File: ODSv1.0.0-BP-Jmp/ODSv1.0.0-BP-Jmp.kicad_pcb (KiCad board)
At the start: 2 copper layers, 150 x 150 mm, 56 parts, among them J1 Conn_01x16, J10 Conn_02x10_Odd_Even, J11 Conn_02x10_Odd_Even, J12 Conn_02x10_Odd_Even, J13 Conn_02x10_Odd_Even, J14 Conn_02x10_Odd_Even, J15 Conn_02x10_Odd_Even, J16 Conn_02x10_Odd_Even, J17 Conn_02x10_Odd_Even, J2 Conn_02x60_Odd_Even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

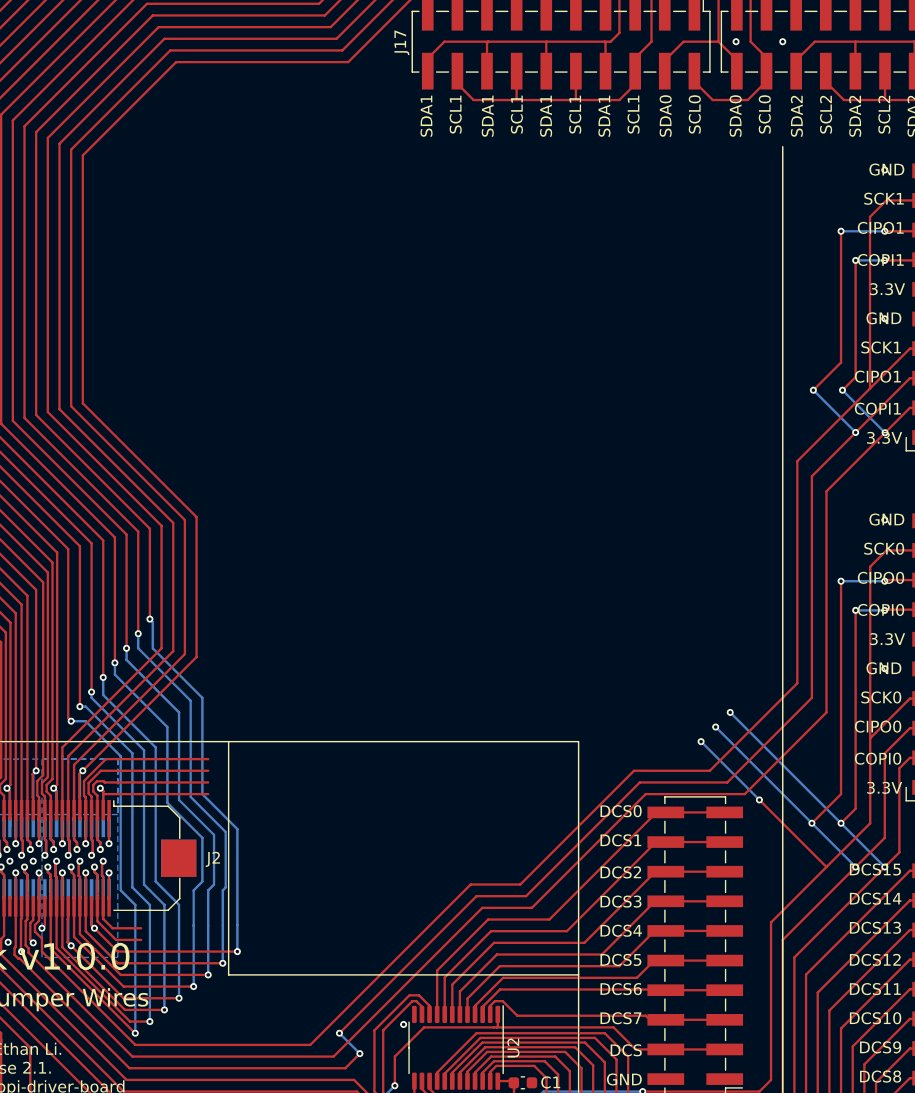
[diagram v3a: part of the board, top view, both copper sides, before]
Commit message: Finish routing I2C headers
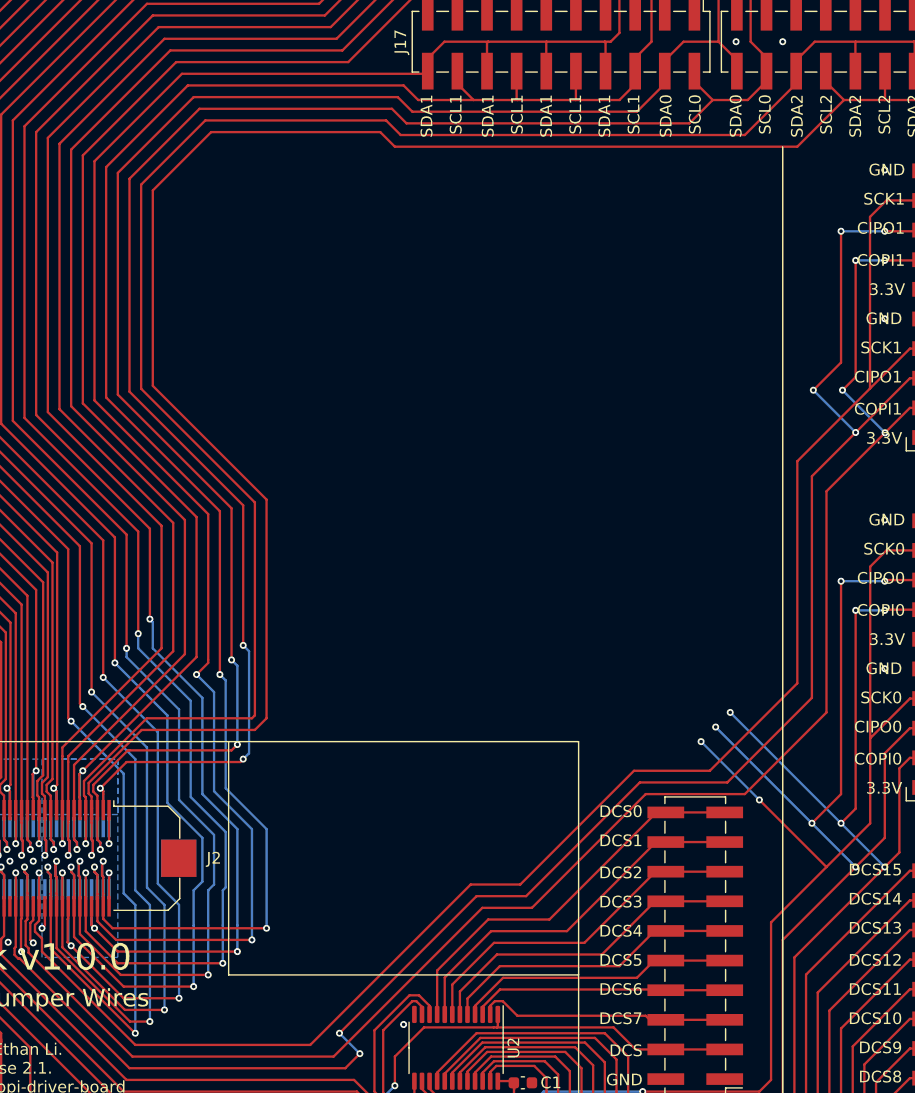
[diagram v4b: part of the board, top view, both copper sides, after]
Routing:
- net /Backbone/I2C2_SCL: track 59.5 -> 179.2 mm
- net /Backbone/I2C2_SDA: track 60.4 -> 177.3 mm
- net /Backbone/I2C1_SCL: track 80.4 -> 197.0 mm, vias 1 -> 3
- net /Backbone/I2C1_SDA: track 84.4 -> 199.1 mm, vias 1 -> 3
- net /Backbone/I2C0_SCL: track 67.4 -> 179.7 mm, vias 1 -> 3
- net /Backbone/I2C0_SDA: track 70.8 -> 179.9 mm, vias 1 -> 3
- net /Backbone/GPIO21: track 152.2 -> 151.4 mm

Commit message: Add a DAC
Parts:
- added C3: 0.047uF, Capacitor_SMD:C_0603_1608Metric, F.Cu at (145.5, 141.8)
- added C4: 0.1uF, Capacitor_SMD:C_0603_1608Metric, F.Cu at (141.2, 144.0)
- added C5: 0.1uF, Capacitor_SMD:C_0603_1608Metric, F.Cu at (142.5, 151.0)
- added C6: 10uF, Capacitor_SMD:C_0603_1608Metric, F.Cu at (142.5, 152.8)
- added C7: 0.1uF, Capacitor_SMD:C_0603_1608Metric, F.Cu at (138.5, 144.5)
- added J18: Conn_02x10_Odd_Even, Connector_PinHeader_2.54mm:PinHeader_2x10_P2.54mm_Vertical_SMD, F.Cu at (119.8, 123.8)
- added J19: Conn_02x10_Odd_Even, Connector_PinHeader_2.54mm:PinHeader_2x10_P2.54mm_Vertical_SMD, F.Cu at (146.2, 123.8)
- added J20: Conn_02x10_Odd_Even, Connector_PinHeader_2.54mm:PinHeader_2x10_P2.54mm_Vertical_SMD, F.Cu at (124.0, 137.8)
- added J21: Conn_02x10_Odd_Even, Connector_PinHeader_2.54mm:PinHeader_2x10_P2.54mm_Vertical_SMD, F.Cu at (126.0, 153.9)
- added J22: Conn_02x10_Odd_Even, Connector_PinHeader_2.54mm:PinHeader_2x10_P2.54mm_Vertical_SMD, F.Cu at (126.0, 169.5)
- added U3: MAX7317, Package_SO:QSOP-16_3.9x4.9mm_P0.635mm, F.Cu at (141.5, 138.2)
- added U4: DACx0508xRTE, Package_DFN_QFN:Texas_S-PWQFN-N16_EP2.1x2.1mm_ThermalVias, F.Cu at (143.2, 147.5)
- moved C2 10.8 mm to (135.2, 194.2)
- moved C1 10.8 mm to (132.8, 204.8)
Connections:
- net /Backbone/SPI0_CIPO renamed /SPI0_CIPO
- net /Backbone/SPI0_COPI renamed /SPI0_COPI
- net /Backbone/SPI0_SCK renamed /SPI0_SCK
- net /Backbone/~DCS0~ renamed /~DCS0~
- net /Backbone/~DCS1~ renamed /~DCS1~
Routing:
- net +3V3: track 730.2 -> 934.7 mm, vias 15 -> 27
- net /Backbone/SPI1_SCK: track 152.3 -> 227.5 mm, vias 1 -> 5
- net /Backbone/SPI1_COPI: track 155.7 -> 230.8 mm, vias 5 -> 7
- net /~DCS1~: track 32.0 -> 100.9 mm, vias 0 -> 2
- net /SPI0_COPI: track 177.0 -> 245.0 mm, vias 8 -> 13
- net /SPI0_CIPO: track 183.0 -> 249.7 mm, vias 8 -> 13
- net /SPI0_SCK: track 171.7 -> 236.2 mm, vias 5 -> 8
- net /Backbone/SPI1_CIPO: track 165.3 -> 227.2 mm
- net /~DCS0~: track 34.0 -> 94.9 mm, vias 0 -> 2
- net /IO Expander/EXPIO0: track 0.00 -> 42.2 mm
- net /IO Expander/EXPIO1: track 0.00 -> 37.8 mm
- net /IO Expander/EXPIO2: track 0.00 -> 33.6 mm
- net /IO Expander/EXPIO3: track 0.00 -> 29.6 mm
- net /IO Expander/DACREF: track 0.00 -> 27.9 mm
- net /IO Expander/EXPIO4: track 0.00 -> 27.6 mm
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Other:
- board text added: "(for ADC)"
- board text added: "(for DAC)"
- board text added: "(for EXP)"
- board text added: "EXP0"
- board text added: "EXP1"
- board text added: "EXP2"
- board text added: "EXP3"
- board text added: "EXP4"
- board text added: "EXP5"
- board text added: "EXP6"
- board text added: "EXP7"
- board text added: "EXP8"
- board text added: "EXP9"

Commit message: Fix footprint and add 3D model for DAC80508, add docs for ICs
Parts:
- U4: footprint Package_DFN_QFN:Texas_S-PWQFN-N16_EP2.1x2.1mm_ThermalVias -> Package_DFN_QFN:WQFN-16-1EP_3x3mm_P0.5mm_EP1.6x1.6mm_ThermalVias
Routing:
- net /~DCS1~: track 100.9 -> 101.6 mm
- net +3V3: track 934.7 -> 935.3 mm
- net /IO Expander/DACREF: track 27.9 -> 28.4 mm
- net /IO Expander/DAC4: track 26.7 -> 27.2 mm
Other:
- board text added: "DAC0"
- board text added: "DAC1"
- board text added: "DAC2"
- board text added: "DAC3"
- board text added: "DAC4"
- board text added: "DAC5"
- board text added: "DAC6"
- board text added: "DAC7"
- board text added: "DACREF"

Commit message: Add an ADC
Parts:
- added C10: 0.1uF, Capacitor_SMD:C_0603_1608Metric, F.Cu at (140.8, 163.0)
- added C11: 10uF, Capacitor_SMD:C_0805_2012Metric, F.Cu at (140.7, 161.0)
- added C8: 0.1uF, Capacitor_SMD:C_0603_1608Metric, F.Cu at (142.2, 159.0)
- added C9: 0.1uF, Capacitor_SMD:C_0603_1608Metric, F.Cu at (148.5, 160.2)
- added U5: AD7689xCP, Package_CSP:LFCSP-20-1EP_4x4mm_P0.5mm_EP2.5x2.5mm, F.Cu at (145.0, 162.5)
- C6: footprint Capacitor_SMD:C_0603_1608Metric -> Capacitor_SMD:C_0805_2012Metric
- moved C5 0.25 mm to (142.5, 150.8)
- moved C6 0.20 mm to (142.3, 152.8)
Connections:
- net /Backbone/~DCS2~ renamed /~DCS2~
- J22 pad 1: (no net) -> /IO Expander/ADCCOM
- J22 pad 10: (no net) -> /IO Expander/ADC4
- J22 pad 11: (no net) -> /IO Expander/ADCCOM
- J22 pad 12: (no net) -> /IO Expander/ADC5
- J22 pad 13: (no net) -> /IO Expander/ADCCOM
- J22 pad 14: (no net) -> /IO Expander/ADC6
- J22 pad 15: (no net) -> /IO Expander/ADCCOM
- J22 pad 16: (no net) -> /IO Expander/ADC7
- J22 pad 17: (no net) -> /IO Expander/ADCCOM
- J22 pad 18: (no net) -> /IO Expander/REF
- J22 pad 19: (no net) -> GND
- J22 pad 2: (no net) -> /IO Expander/ADC0
- J22 pad 20: (no net) -> /IO Expander/REFIN
- J22 pad 3: (no net) -> /IO Expander/ADCCOM
- J22 pad 4: (no net) -> /IO Expander/ADC1
- J22 pad 5: (no net) -> /IO Expander/ADCCOM
- J22 pad 6: (no net) -> /IO Expander/ADC2
- J22 pad 7: (no net) -> /IO Expander/ADCCOM
- J22 pad 8: (no net) -> /IO Expander/ADC3
- J22 pad 9: (no net) -> /IO Expander/ADCCOM
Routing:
- net /IO Expander/ADC0: track 0.00 -> 39.8 mm
- net /IO Expander/ADC1: track 0.00 -> 36.3 mm
- net /IO Expander/ADCCOM: track 0.00 -> 35.6 mm
- net /IO Expander/ADC2: track 0.00 -> 32.7 mm
- net /IO Expander/ADC3: track 0.00 -> 29.0 mm
- net /IO Expander/ADC4: track 0.00 -> 22.1 mm
- net /IO Expander/ADC5: track 0.00 -> 20.3 mm
- net /SPI0_COPI: track 245.4 -> 265.6 mm, vias 13 -> 14
- net +3V3: track 935.3 -> 954.4 mm, vias 27 -> 29
- net /IO Expander/ADC6: track 0.00 -> 18.2 mm
- net /~DCS1~: track 101.6 -> 83.7 mm
- net /SPI0_SCK: track 236.6 -> 253.6 mm, vias 8 -> 10
- net /IO Expander/ADC7: track 0.00 -> 16.2 mm
- net /SPI0_CIPO: track 250.2 -> 265.8 mm, vias 13 -> 14
- net /~DCS2~: track 29.9 -> 45.0 mm, vias 0 -> 2
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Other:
- board text added: "ADC0"
- board text added: "ADC1"
- board text added: "ADC2"
- board text added: "ADC3"
- board text added: "ADC4"
- board text added: "ADC5"
- board text added: "ADC6"
- board text added: "ADC7"
- board text added: "ADCCOM"
- board text added: "REF"
- board text added: "REFIN"
